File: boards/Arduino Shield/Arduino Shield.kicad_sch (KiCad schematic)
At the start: 11 parts, among them J1 Screw_Terminal_01x09, J10 Screw_Terminal_01x04, J2 Screw_Terminal_01x09, J3 Screw_Terminal_01x09, J4 Screw_Terminal_01x09, J5 Screw_Terminal_01x09, J6 Screw_Terminal_01x09, J7 Screw_Terminal_01x09, J8 Screw_Terminal_01x09, J9 Screw_Terminal_01x09, U1 A000062

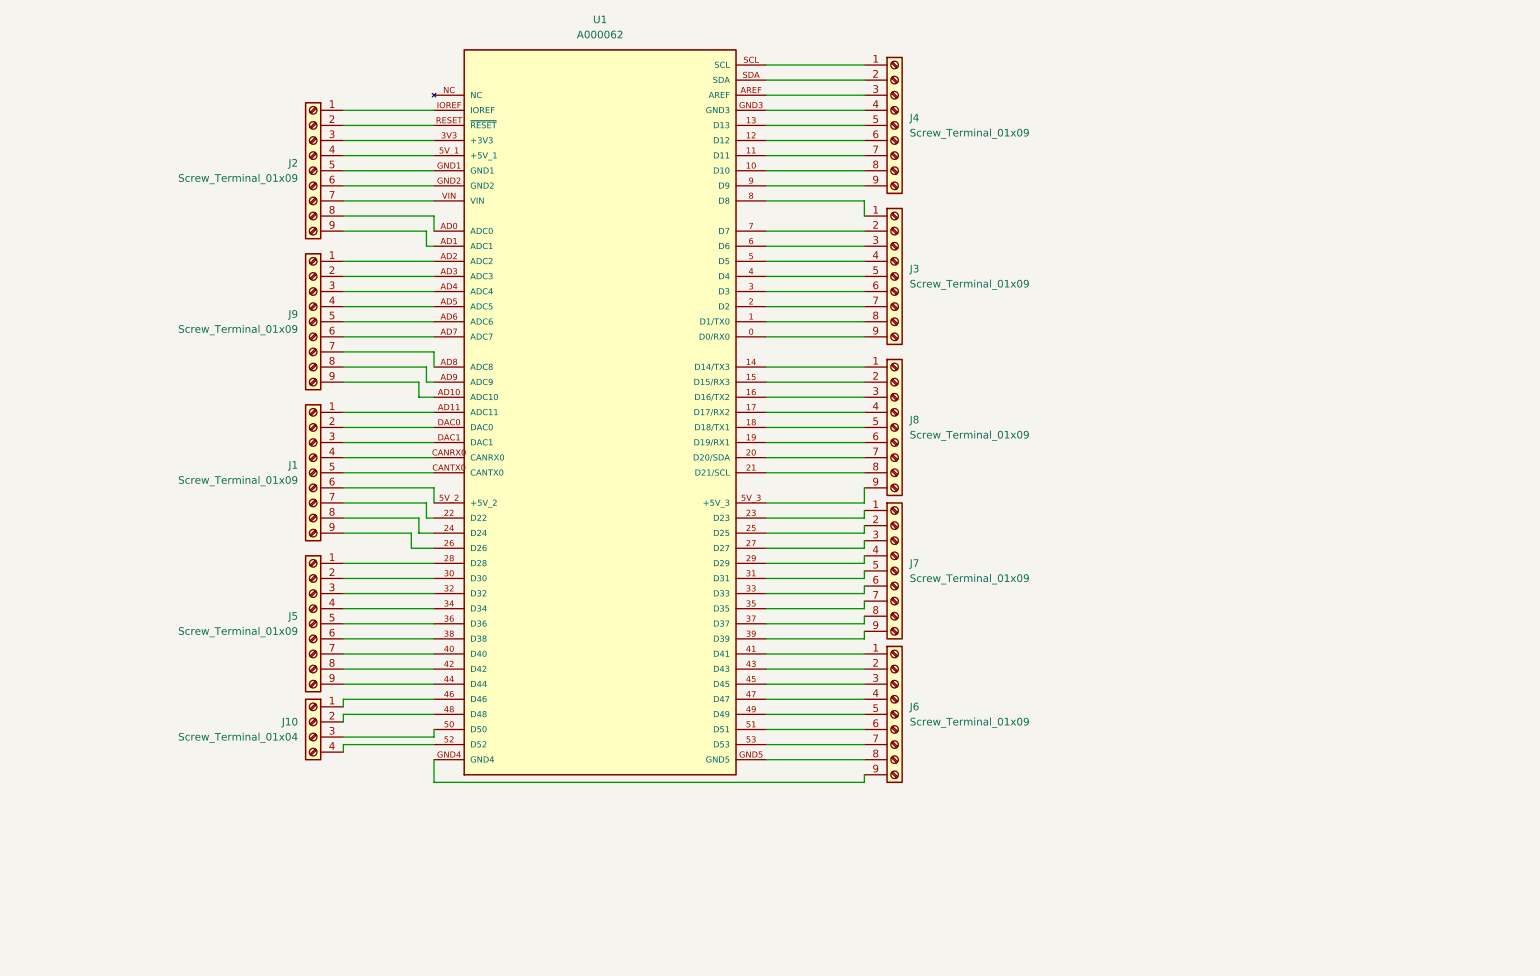
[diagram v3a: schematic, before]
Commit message: Terminal Blocls Update
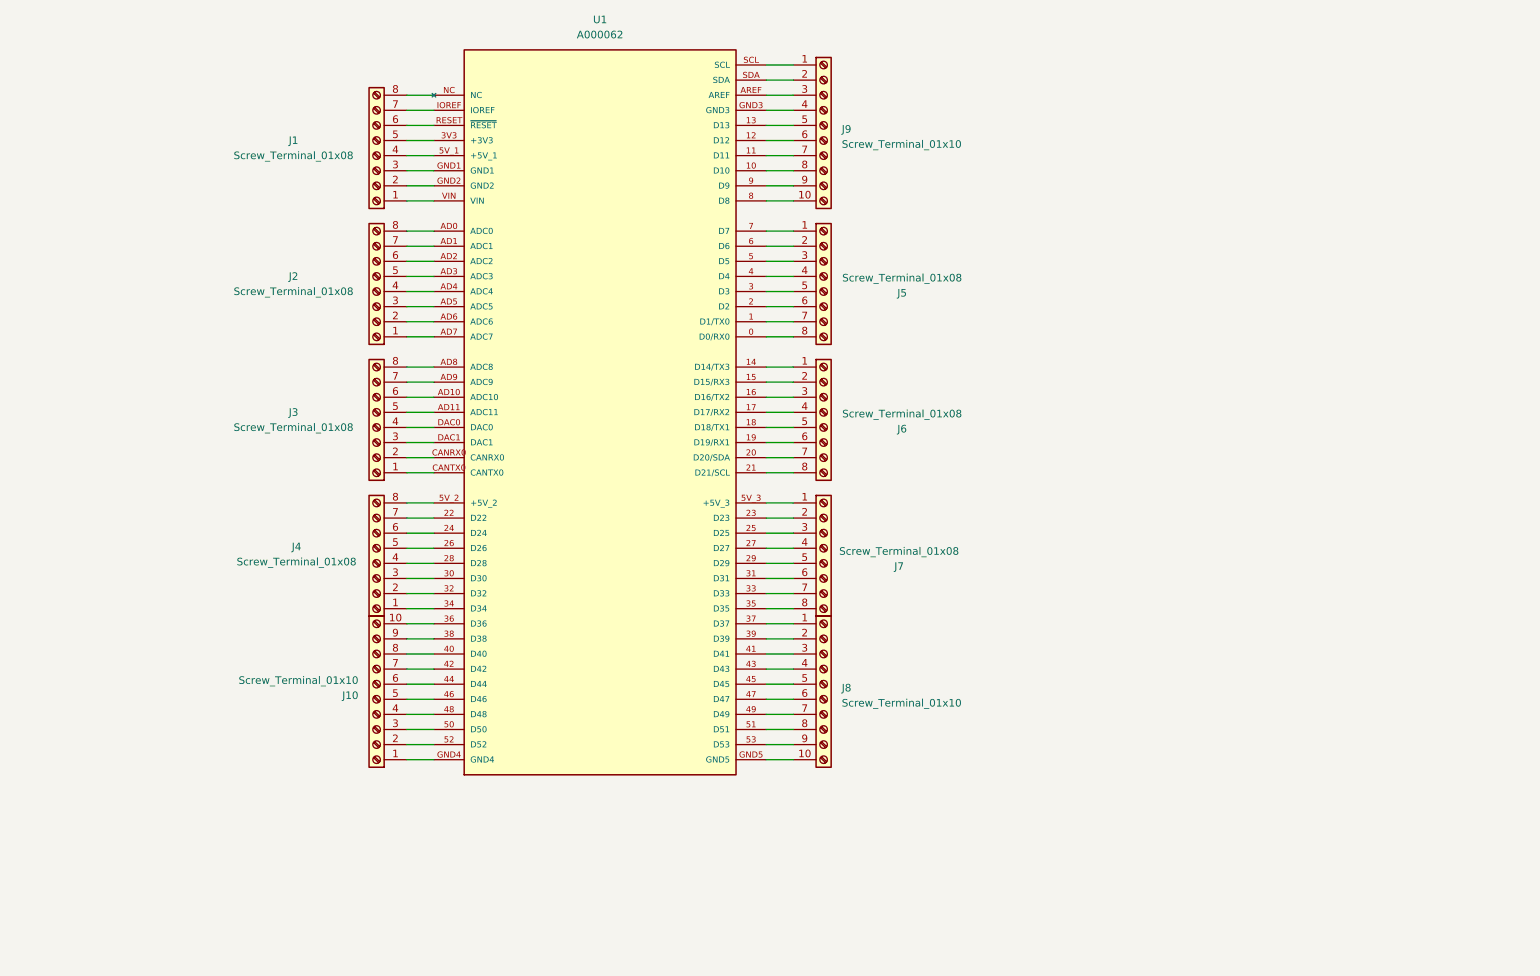
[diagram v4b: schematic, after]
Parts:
- removed J1, J2, J3, J4, J5, J6, J7, J8, J9: Screw_Terminal_01x09, TerminalBlock_4Ucon:TerminalBlock_4Ucon_1x09_P3.50mm_Horizontal, symbol Connector:Screw_Terminal_01x09
- removed J10: Screw_Terminal_01x04, TerminalBlock_4Ucon:TerminalBlock_4Ucon_1x04_P3.50mm_Horizontal, symbol Connector:Screw_Terminal_01x04
- added J1, J2, J3, J4, J5, J6, J7: Screw_Terminal_01x08, symbol Connector:Screw_Terminal_01x08
- added J10, J8, J9: Screw_Terminal_01x10, symbol Connector:Screw_Terminal_01x10
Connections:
- net at U1.IOREF: now also J1.7 (Pin_7)
- net at U1.RESET (~{RESET}): now also J1.6 (Pin_6)
- net at U1.3V3 (+3V3): now also J1.5 (Pin_5)
- net at U1.5V_1 (+5V_1): now also J1.4 (Pin_4)
- net at U1.GND1: now also J1.3 (Pin_3)
- net at U1.GND2: now also J1.2 (Pin_2)
- net at U1.VIN: now also J1.1 (Pin_1)
- net at U1.AD0 (ADC0): now also J2.8 (Pin_8)
- net at U1.AD1 (ADC1): now also J2.7 (Pin_7)
- net at U1.AD11 (ADC11): now also J3.5 (Pin_5)
- net at U1.DAC0: now also J3.4 (Pin_4)
- net at U1.DAC1: now also J3.3 (Pin_3)
- net at U1.CANRX0: now also J3.2 (Pin_2)
- net at U1.CANTX0: now also J3.1 (Pin_1)
- net at U1.5V_2 (+5V_2): now also J4.8 (Pin_8)
- net at U1.22 (D22): now also J4.7 (Pin_7)
- net at U1.24 (D24): now also J4.6 (Pin_6)
- net at U1.26 (D26): now also J4.5 (Pin_5)
- net at U1.8 (D8): now also J9.10 (Pin_10)
- net at U1.7 (D7): now also J5.1 (Pin_1)
- net at U1.6 (D6): now also J5.2 (Pin_2)
- net at U1.5 (D5): now also J5.3 (Pin_3)
- net at U1.4 (D4): now also J5.4 (Pin_4)
- net at U1.3 (D3): now also J5.5 (Pin_5)
- net at U1.2 (D2): now also J5.6 (Pin_6)
- net at U1.1 (D1/TX0): now also J5.7 (Pin_7)
- net at U1.0 (D0/RX0): now also J5.8 (Pin_8)
- net at U1.SCL: now also J9.1 (Pin_1)
- net at U1.SDA: now also J9.2 (Pin_2)
- net at U1.AREF: now also J9.3 (Pin_3)
- net at U1.GND3: now also J9.4 (Pin_4)
- net at U1.13 (D13): now also J9.5 (Pin_5)
- net at U1.12 (D12): now also J9.6 (Pin_6)
- net at U1.11 (D11): now also J9.7 (Pin_7)
- net at U1.10 (D10): now also J9.8 (Pin_8)
- net at U1.9 (D9): now also J9.9 (Pin_9)
- net at U1.23 (D23): now also J7.2 (Pin_2)
- net at U1.25 (D25): now also J7.3 (Pin_3)
- net at U1.27 (D27): now also J7.4 (Pin_4)
- net at U1.29 (D29): now also J7.5 (Pin_5)
- net at U1.31 (D31): now also J7.6 (Pin_6)
- net at U1.33 (D33): now also J7.7 (Pin_7)
- net at U1.35 (D35): now also J7.8 (Pin_8)
- net at U1.37 (D37): now also J8.1 (Pin_1)
- net at U1.39 (D39): now also J8.2 (Pin_2)
- net at U1.41 (D41): now also J8.3 (Pin_3)
- net at U1.43 (D43): now also J8.4 (Pin_4)
- net at U1.45 (D45): now also J8.5 (Pin_5)
- net at U1.47 (D47): now also J8.6 (Pin_6)
- net at U1.49 (D49): now also J8.7 (Pin_7)
- net at U1.51 (D51): now also J8.8 (Pin_8)
- net at U1.53 (D53): now also J8.9 (Pin_9)
- net at U1.GND5: now also J8.10 (Pin_10)
- net at U1.GND4: now also J10.1 (Pin_1)
- net at U1.46 (D46): now also J10.5 (Pin_5)
- net at U1.48 (D48): now also J10.4 (Pin_4)
- net at U1.50 (D50): now also J10.3 (Pin_3)
- net at U1.52 (D52): now also J10.2 (Pin_2)
- net at U1.28 (D28): now also J4.4 (Pin_4)
- net at U1.30 (D30): now also J4.3 (Pin_3)
- net at U1.32 (D32): now also J4.2 (Pin_2)
- net at U1.34 (D34): now also J4.1 (Pin_1)
- net at U1.36 (D36): now also J10.10 (Pin_10)
- net at U1.38 (D38): now also J10.9 (Pin_9)
- net at U1.40 (D40): now also J10.8 (Pin_8)
- net at U1.42 (D42): now also J10.7 (Pin_7)
- net at U1.44 (D44): now also J10.6 (Pin_6)
- net at U1.AD2 (ADC2): now also J2.6 (Pin_6)
- net at U1.AD3 (ADC3): now also J2.5 (Pin_5)
- net at U1.AD4 (ADC4): now also J2.4 (Pin_4)
- net at U1.AD5 (ADC5): now also J2.3 (Pin_3)
- net at U1.AD6 (ADC6): now also J2.2 (Pin_2)
- net at U1.AD7 (ADC7): now also J2.1 (Pin_1)
- net at U1.AD8 (ADC8): now also J3.8 (Pin_8)
- net at U1.AD9 (ADC9): now also J3.7 (Pin_7)
- net at U1.AD10 (ADC10): now also J3.6 (Pin_6)
- net at U1.14 (D14/TX3): now also J6.1 (Pin_1)
- net at U1.15 (D15/RX3): now also J6.2 (Pin_2)
- net at U1.16 (D16/TX2): now also J6.3 (Pin_3)
- net at U1.17 (D17/RX2): now also J6.4 (Pin_4)
- net at U1.18 (D18/TX1): now also J6.5 (Pin_5)
- net at U1.19 (D19/RX1): now also J6.6 (Pin_6)
- net at U1.20 (D20/SDA): now also J6.7 (Pin_7)
- net at U1.21 (D21/SCL): now also J6.8 (Pin_8)
- net at U1.5V_3 (+5V_3): now also J7.1 (Pin_1)
- net at U1.NC: now also J1.8 (Pin_8)

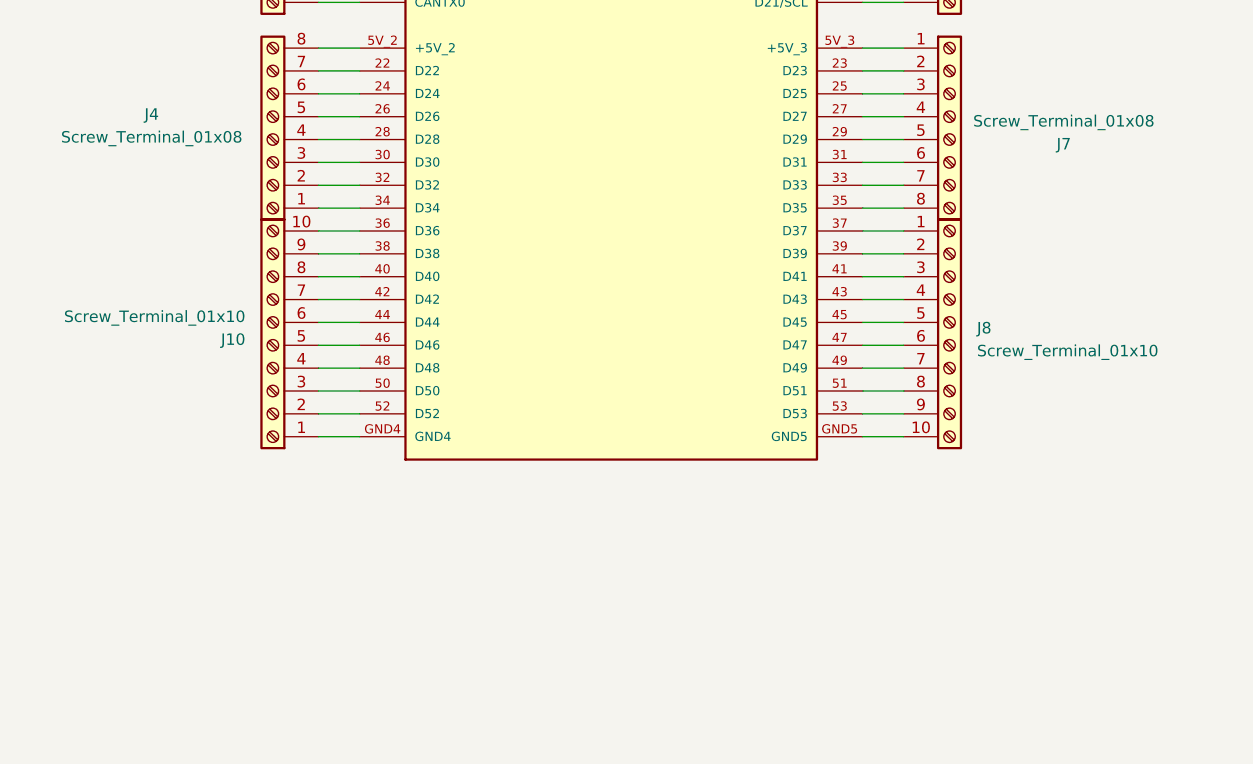
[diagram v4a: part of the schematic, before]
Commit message: Added LEDs
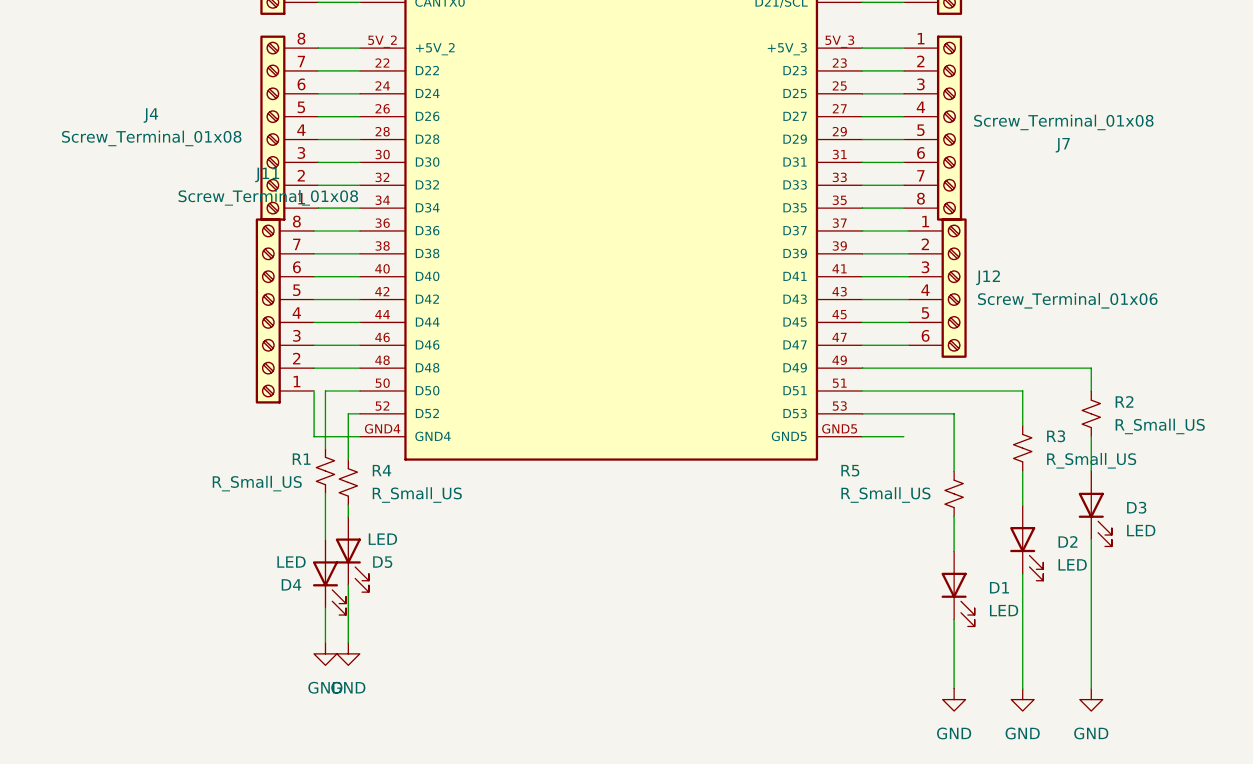
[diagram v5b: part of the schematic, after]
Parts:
- removed J10, J8: Screw_Terminal_01x10, symbol Connector:Screw_Terminal_01x10
- added D1, D2, D3, D4, D5: LED, symbol Device:LED
- added J11: Screw_Terminal_01x08, symbol Connector:Screw_Terminal_01x08
- added J12: Screw_Terminal_01x06, symbol Connector:Screw_Terminal_01x06
- added R1, R2, R3, R4, R5: R_Small_US, symbol Device:R_Small_US
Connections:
- net at U1.37 (D37): now also J12.1 (Pin_1)
- net at U1.39 (D39): now also J12.2 (Pin_2)
- net at U1.41 (D41): now also J12.3 (Pin_3)
- net at U1.43 (D43): now also J12.4 (Pin_4)
- net at U1.45 (D45): now also J12.5 (Pin_5)
- net at U1.47 (D47): now also J12.6 (Pin_6)
- net at U1.49 (D49): now also R2.2
- net at U1.51 (D51): now also R3.2
- net at U1.53 (D53): now also R5.2
- net at U1.GND4: now also J11.1 (Pin_1)
- net at U1.36 (D36): now also J11.8 (Pin_8)
- net at U1.52 (D52): now also R4.2
- net at U1.50 (D50): now also R1.2
- net at U1.48 (D48): now also J11.2 (Pin_2)
- net at U1.46 (D46): now also J11.3 (Pin_3)
- net at U1.44 (D44): now also J11.4 (Pin_4)
- net at U1.42 (D42): now also J11.5 (Pin_5)
- net at U1.40 (D40): now also J11.6 (Pin_6)
- net at U1.38 (D38): now also J11.7 (Pin_7)
- new net: D1.2 (A), R5.1
- new net: D5.2 (A), R4.1
- new net: D3.2 (A), R2.1
- new net: D2.2 (A), R3.1
- new net: D4.2 (A), R1.1
- new net GND: D1.1 (K), D2.1 (K), D3.1 (K), D4.1 (K), D5.1 (K)
